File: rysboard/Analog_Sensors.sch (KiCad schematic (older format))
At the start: 16 parts

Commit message: cleanup
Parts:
- added D18, D19, D20: D_TVS, symbol Device:D_TVS
- added R62, R63, R64, R65, R66, R67: R, symbol Device:R
- J14: renamed from J?; value Conn_01x02 -> BAT2_TH
- J21: renamed from J?; value Conn_01x02 -> BAT3_TH
- J8: renamed from J?; value Conn_01x02 -> BAT1_TH
- gave numbers to parts that had none: 13
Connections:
- net BAT_T_1: now also J8.2 (Pin_2), R54.2
- net BAT_T_2: now also J14.2 (Pin_2), R58.2
- net BAT_T_3: now also J21.2 (Pin_2), R60.2
- net BOARD_T_1: now also R55.2, TH2.1
- net BOARD_T_2: now also R59.2, TH3.1
- net BOARD_T_3: now also R61.2, TH4.1
- net GND: now also J14.1 (Pin_1), J21.1 (Pin_1), J8.1 (Pin_1), D18.2 (A2), D19.2 (A2), D20.2 (A2), R63.2, R65.2, R67.2; no longer J14.2 (Pin_2), J21.2 (Pin_2), J8.2 (Pin_2)
- net V_BAT_C1: now also D18.1 (A1), R62.2, R63.1
- net V_BAT_C2: now also D19.1 (A1), R64.2, R65.1
- net V_BAT_C3: now also D20.1 (A1), R66.2, R67.1
- net V_CELL1: now also R62.1
- net V_CELL2: now also R64.1
- net V_CELL3: now also R66.1
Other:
- note added: "0-10V\n"
- note added: "0-15V\n"
- note added: "0-5V\n"
- moved on the sheet: R54, R58, R60

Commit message: first modyfications in St Motor section
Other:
- note added: "33v == 3.3v\n\nR=U/I\nI=U/R1+R2\nR1 =90KOhm\nR2 = 10KOhm\n\n9.9 == 3.3V\nR1 = 10KOhm\nR2 = 5KOhm"
- note removed: "33v == 3.3v\n\nR=U/I\nI=U/R1+R2\nR1 =10KOhm\nR2 = 90KOhm\n\n9.9 == 3.3V\nR1 = 10KOhm\nR2 = 20 KOhm"
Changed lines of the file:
@@
 $EndComp
 Text Notes 3950 4850 0    50   ~ 0
-33v == 3.3v\n\nR=U/I\nI=U/R1+R2\nR1 =10KOhm\nR2 = 90KOhm\n\n9.9 == 3.3V\nR1 = 10KOhm\nR2 =  20 KOhm
+33v == 3.3v\n\nR=U/I\nI=U/R1+R2\nR1 =90KOhm\nR2 = 10KOhm\n\n9.9 == 3.3V\nR1 = 10KOhm\nR2 =  5KOhm
 Text Notes 3900 3900 0    50   ~ 0
 TO DO:\nDouble check values\n

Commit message: sensors enable added, Vref problem to solve
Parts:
- removed D18, D19, D20: D_TVS, symbol Device:D_TVS
- removed R55, R56, R57, R59, R61, R64, R66: R, symbol Device:R
- added Q?: IRLML6402, Package_TO_SOT_SMD:SOT-23, symbol Transistor_FET:IRLML6402
- added R? (x7): 10KR, symbol Device:R
- added R?: 5KR, symbol Device:R
- added R?: 100KR, symbol Device:R
- R52: value 90KR0.5% -> 9KR0.5%
- R53: value 10KR0.5% -> 1KR0.5%
- R62: value R -> 10KR
- R63: value R -> 20KR
- R65: value R -> 5KR
- R67: value R -> 2.8KR
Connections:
- net +5V: now also R?.1
- net BOARD_T_1: now also R?.2
- net BOARD_T_2: now also R?.2
- net BOARD_T_3: now also R?.2
- net GND: now also R?.2
- net MCU_3.3V: now also Q?.2 (S), R?.1; no longer R54.1, R58.1, R60.1
- net V_BAT_C2: now also R?.2
- net V_BAT_C3: now also R?.2
- net V_CELL2: now also R?.1
- net V_CELL3: now also R?.1
- net V_P_5: now also R?.1, R?.2
- new net: Q?.1 (G), R?.1, R?.2
- new net MCU_Sensor_3.3V: Q?.3 (D), R54.1, R58.1, R60.1, R?.1, R?.1, R?.1
- new net S_E: R?.2
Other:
- note added: "0-15.086V\n"
- note added: "0-4.95V\n"
- note added: "0-9.9V\n"
- note added: "When not used, thermistors do not need to be powered on."
- note removed: "0-10V\n"
- note removed: "0-15V\n"
- note removed: "0-5V\n"
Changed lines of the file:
@@
 	1    0    0    -1
 $EndComp
-Text GLabel 3350 950  1    50   Output ~ 0
-MCU_3.3V
-Text GLabel 2550 950  1    50   Output ~ 0
-MCU_3.3V
-Text GLabel 4150 950  1    50   Output ~ 0
-MCU_3.3V
 $Comp
 L Connector_Generic:Conn_01x02 J8
@@
 	0    -1   -1   0
 $EndComp
-$Comp
-L Device:R R55
-U 1 1 603EEB5E
-P 2750 2200
-F 0 "R55" H 2820 2246 50  0000 L CNN
-F 1 "R" H 2820 2155 50  0000 L CNN
-F 2 "" V 2680 2200 50  0001 C CNN
-F 3 "~" H 2750 2200 50  0001 C CNN
-	1    2750 2200
-	1    0    0    -1
-$EndComp
-Text GLabel 2600 2000 0    50   Output ~ 0
-MCU_3.3V
-$Comp
-L Device:R R59
-U 1 1 603EEFA0
-P 3400 2200
-F 0 "R59" H 3470 2246 50  0000 L CNN
-F 1 "R" H 3470 2155 50  0000 L CNN
-F 2 "" V 3330 2200 50  0001 C CNN
-F 3 "~" H 3400 2200 50  0001 C CNN
-	1    3400 2200
-	1    0    0    -1
-$EndComp
-$Comp
-L Device:R R61
-U 1 1 603EF182
-P 4200 2200
-F 0 "R61" H 4270 2246 50  0000 L CNN
-F 1 "R" H 4270 2155 50  0000 L CNN
-F 2 "" V 4130 2200 50  0001 C CNN
-F 3 "~" H 4200 2200 50  0001 C CNN
-	1    4200 2200
-	1    0    0    -1
-$EndComp
 Wire Wire Line
 	2600 2000 2750 2000
@@
 P 2050 4400
 F 0 "R52" H 2120 4446 50  0000 L CNN
-F 1 "90KR0.5%" H 2120 4355 50  0000 L CNN
+F 1 "9KR0.5%" H 2120 4355 50  0000 L CNN
 F 2 "" V 1980 4400 50  0001 C CNN
 F 3 "~" H 2050 4400 50  0001 C CNN
@@
 P 2050 4700
 F 0 "R53" H 1980 4654 50  0000 R CNN
-F 1 "10KR0.5%" H 1980 4745 50  0000 R CNN
+F 1 "1KR0.5%" H 1980 4745 50  0000 R CNN
 F 2 "" V 1980 4700 50  0001 C CNN
 F 3 "~" H 2050 4700 50  0001 C CNN
@@
 Connection ~ 2050 4550
 $Comp
-L Device:R R56
-U 1 1 60408D6C
-P 3150 4400
-F 0 "R56" H 3220 4446 50  0000 L CNN
-F 1 "R" H 3220 4355 50  0000 L CNN
-F 2 "" V 3080 4400 50  0001 C CNN
-F 3 "~" H 3150 4400 50  0001 C CNN
-	1    3150 4400
-	1    0    0    -1
-$EndComp
-$Comp
-L Device:R R57
-U 1 1 604091C5
-P 3150 4700
-F 0 "R57" H 3220 4746 50  0000 L CNN
-F 1 "R" H 3220 4655 50  0000 L CNN
-F 2 "" V 3080 4700 50  0001 C CNN
-F 3 "~" H 3150 4700 50  0001 C CNN
-	1    3150 4700
-	1    0    0    -1
-$EndComp
-Connection ~ 3150 4550
-$Comp
 L power:GND #PWR052
 U 1 1 604093E1
@@
 P 6250 4400
 F 0 "R62" H 6320 4446 50  0000 L CNN
-F 1 "R" H 6320 4355 50  0000 L CNN
+F 1 "10KR" H 6320 4355 50  0000 L CNN
 F 2 "" V 6180 4400 50  0001 C CNN
 F 3 "~" H 6250 4400 50  0001 C CNN
@@
 P 6250 4700
 F 0 "R63" H 6320 4746 50  0000 L CNN
-F 1 "R" H 6320 4655 50  0000 L CNN
+F 1 "20KR" H 6320 4655 50  0000 L CNN
 F 2 "" V 6180 4700 50  0001 C CNN
 F 3 "~" H 6250 4700 50  0001 C CNN
 	1    6250 4700
-	1    0    0    -1
-$EndComp
-$Comp
-L Device:R R64
-U 1 1 6037FF91
-P 7050 4400
-F 0 "R64" H 7120 4446 50  0000 L CNN
-F 1 "R" H 7120 4355 50  0000 L CNN
-F 2 "" V 6980 4400 50  0001 C CNN
-F 3 "~" H 7050 4400 50  0001 C CNN
-	1    7050 4400
 	1    0    0    -1
 $EndComp
@@
 P 7050 4700
 F 0 "R65" H 7120 4746 50  0000 L CNN
-F 1 "R" H 7120 4655 50  0000 L CNN
+F 1 "5KR" H 7120 4655 50  0000 L CNN
 F 2 "" V 6980 4700 50  0001 C CNN
 F 3 "~" H 7050 4700 50  0001 C CNN
 	1    7050 4700
-	1    0    0    -1
-$EndComp
-$Comp
-L Device:R R66
-U 1 1 603802FE
-P 7850 4400
-F 0 "R66" H 7920 4446 50  0000 L CNN
-F 1 "R" H 7920 4355 50  0000 L CNN
-F 2 "" V 7780 4400 50  0001 C CNN
-F 3 "~" H 7850 4400 50  0001 C CNN
-	1    7850 4400
 	1    0    0    -1
 $EndComp
@@
 P 7850 4700
 F 0 "R67" H 7920 4746 50  0000 L CNN
-F 1 "R" H 7920 4655 50  0000 L CNN
+F 1 "2.8KR" H 7920 4655 50  0000 L CNN
 F 2 "" V 7780 4700 50  0001 C CNN
 F 3 "~" H 7850 4700 50  0001 C CNN
@@
 $EndComp
 Text Notes 6250 3650 0    50   ~ 0
-0-5V\n
+0-4.95V\n
 Text Notes 6950 3650 0    50   ~ 0
-0-10V\n
+0-9.9V\n
 Text Notes 7750 3650 0    50   ~ 0
-0-15V\n
-$Comp
-L Device:D_TVS D18
-U 1 1 60385CF5
-P 6500 4700
-F 0 "D18" V 6454 4780 50  0000 L CNN
-F 1 "D_TVS" V 6545 4780 50  0000 L CNN
-F 2 "" H 6500 4700 50  0001 C CNN
-F 3 "~" H 6500 4700 50  0001 C CNN
-	1    6500 4700
-	0    1    1    0
-$EndComp
-$Comp
-L Device:D_TVS D19
-U 1 1 603861A1
-P 7300 4700
-F 0 "D19" V 7254 4780 50  0000 L CNN
-F 1 "D_TVS" V 7345 4780 50  0000 L CNN
-F 2 "" H 7300 4700 50  0001 C CNN
-F 3 "~" H 7300 4700 50  0001 C CNN
-	1    7300 4700
-	0    1    1    0
-$EndComp
-$Comp
-L Device:D_TVS D20
-U 1 1 6038637D
-P 8100 4700
-F 0 "D20" V 8054 4780 50  0000 L CNN
-F 1 "D_TVS" V 8145 4780 50  0000 L CNN
-F 2 "" H 8100 4700 50  0001 C CNN
-F 3 "~" H 8100 4700 50  0001 C CNN
-	1    8100 4700
-	0    1    1    0
-$EndComp
-Wire Wire Line
-	8100 4850 7850 4850
-Connection ~ 7850 4850
-Wire Wire Line
-	8100 4550 7850 4550
-Connection ~ 7850 4550
-Wire Wire Line
-	7300 4550 7050 4550
-Connection ~ 7050 4550
-Wire Wire Line
-	7300 4850 7050 4850
-Connection ~ 7050 4850
-Wire Wire Line
-	6500 4550 6250 4550
-Connection ~ 6250 4550
-Wire Wire Line
-	6500 4850 6250 4850
-Connection ~ 6250 4850
+0-15.086V\n
 Text HLabel 2500 1300 0    50   Input ~ 0
 BAT_T_1
@@
 	4150 1300 4150 1350
 Connection ~ 4150 1300
+$Comp
+L Device:R R?
+U 1 1 603B8902
+P 7050 4400
+F 0 "R?" H 7120 4446 50  0000 L CNN
+F 1 "10KR" H 7120 4355 50  0000 L CNN
+F 2 "" V 6980 4400 50  0001 C CNN
+F 3 "~" H 7050 4400 50  0001 C CNN
+	1    7050 4400
+	1    0    0    -1
+$EndComp
+$Comp
+L Device:R R?
+U 1 1 603B8D2E
+P 7850 4400
+F 0 "R?" H 7920 4446 50  0000 L CNN
+F 1 "10KR" H 7920 4355 50  0000 L CNN
+F 2 "" V 7780 4400 50  0001 C CNN
+F 3 "~" H 7850 4400 50  0001 C CNN
+	1    7850 4400
+	1    0    0    -1
+$EndComp
+$Comp
+L Device:R R?
+U 1 1 603B9257
+P 3150 4400
+F 0 "R?" H 3220 4446 50  0000 L CNN
+F 1 "10KR" H 3220 4355 50  0000 L CNN
+F 2 "" V 3080 4400 50  0001 C CNN
+F 3 "~" H 3150 4400 50  0001 C CNN
+	1    3150 4400
+	1    0    0    -1
+$EndComp
+$Comp
+L Device:R R?
+U 1 1 603B976E
+P 3150 4700
+F 0 "R?" H 3220 4746 50  0000 L CNN
+F 1 "5KR" H 3220 4655 50  0000 L CNN
+F 2 "" V 3080 4700 50  0001 C CNN
+F 3 "~" H 3150 4700 50  0001 C CNN
+	1    3150 4700
+	1    0    0    -1
+$EndComp
+Connection ~ 3150 4550
+Text GLabel 6150 1100 1    50   Output ~ 0
+MCU_3.3V
+Text Label 2600 2000 0    50   ~ 0
+MCU_Sensor_3.3V
+Text Label 1900 900  0    50   ~ 0
+MCU_Sensor_3.3V
+Wire Wire Line
+	1900 900  2550 900
+Wire Wire Line
+	2550 900  2550 950
+Text Label 2750 900  0    50   ~ 0
+MCU_Sensor_3.3V
+Wire Wire Line
+	2750 900  3350 900
+Wire Wire Line
+	3350 900  3350 950
+Text Label 3550 900  0    50   ~ 0
+MCU_Sensor_3.3V
+Wire Wire Line
+	3550 900  4150 900
+Wire Wire Line
+	4150 900  4150 950
+Text Label 7150 1600 0    50   ~ 0
+MCU_Sensor_3.3V
+$Comp
+L Device:R R?
+U 1 1 603BD637
+P 2750 2200
+F 0 "R?" H 2820 2246 50  0000 L CNN
+F 1 "10KR" H 2820 2155 50  0000 L CNN
+F 2 "" V 2680 2200 50  0001 C CNN
+F 3 "~" H 2750 2200 50  0001 C CNN
+	1    2750 2200
+	1    0    0    -1
+$EndComp
+$Comp
+L Device:R R?
+U 1 1 603BDD9E
+P 3400 2200
+F 0 "R?" H 3470 2246 50  0000 L CNN
+F 1 "10KR" H 3470 2155 50  0000 L CNN
+F 2 "" V 3330 2200 50  0001 C CNN
+F 3 "~" H 3400 2200 50  0001 C CNN
+	1    3400 2200
+	1    0    0    -1
+$EndComp
+$Comp
+L Device:R R?
+U 1 1 603BDFD4
+P 4200 2200
+F 0 "R?" H 4270 2246 50  0000 L CNN
+F 1 "10KR" H 4270 2155 50  0000 L CNN
+F 2 "" V 4130 2200 50  0001 C CNN
+F 3 "~" H 4200 2200 50  0001 C CNN
+	1    4200 2200
+	1    0    0    -1
+$EndComp
+$Comp
+L Transistor_FET:IRLML6402 Q?
+U 1 1 603BF81C
+P 6650 1400
+F 0 "Q?" H 6854 1354 50  0000 L CNN
+F 1 "IRLML6402" H 6854 1445 50  0000 L CNN
+F 2 "Package_TO_SOT_SMD:SOT-23" H 6850 1325 50  0001 L CIN
+F 3 "https://www.infineon.com/dgdl/irlml6402pbf.pdf?fileId=5546d462533600a401535668d5c2263c" H 6650 1400 50  0001 L CNN
+	1    6650 1400
+	1    0    0    1
+$EndComp
+Wire Wire Line
+	7150 1600 6750 1600
+Wire Wire Line
+	6150 1100 6300 1100
+Wire Wire Line
+	6750 1100 6750 1200
+$Comp
+L Device:R R?
+U 1 1 603C19CD
+P 6300 1250
+F 0 "R?" H 6370 1296 50  0000 L CNN
+F 1 "100KR" H 6370 1205 50  0000 L CNN
+F 2 "" V 6230 1250 50  0001 C CNN
+F 3 "~" H 6300 1250 50  0001 C CNN
+	1    6300 1250
+	1    0    0    -1
+$EndComp
+Connection ~ 6300 1100
+Wire Wire Line
+	6300 1100 6750 1100
+$Comp
+L Device:R R?
+U 1 1 603C1DE2
+P 6150 1400
+F 0 "R?" H 6220 1446 50  0000 L CNN
+F 1 "10KR" H 6220 1355 50  0000 L CNN
+F 2 "" V 6080 1400 50  0001 C CNN
+F 3 "~" H 6150 1400 50  0001 C CNN
+	1    6150 1400
+	0    1    1    0
+$EndComp
+Wire Wire Line
+	6300 1400 6450 1400
+Connection ~ 6300 1400
+Text HLabel 5850 1400 0    50   Input ~ 0
+S_E
+Wire Wire Line
+	5850 1400 6000 1400
+Text Notes 8450 1000 0    50   ~ 0
+When not used, thermistors do not need to be powered on.
 $EndSCHEMATC

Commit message: new mosfet footprints
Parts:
- R52, R53, R62, R63, R65, R67: footprint (none) -> Resistor_SMD:R_0603_1608Metric
- R54, R58, R60: value R -> 10KR; footprint (none) -> Resistor_SMD:R_0603_1608Metric
- R55, R56, R57, R59, R61, R64, R66, R70, R71: renamed from R?; footprint (none) -> Resistor_SMD:R_0603_1608Metric
- TH2, TH3, TH4: footprint (none) -> Resistor_SMD:R_0805_2012Metric_Pad1.15x1.40mm_HandSolder
- gave numbers to parts that had none: 1
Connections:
- net MCU_Sensor_3.3V renamed 3_3V_REF
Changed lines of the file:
@@
 V_BAT_C3
-$Comp
-L Device:R R54
-U 1 1 603E581F
-P 2550 1100
-F 0 "R54" H 2620 1146 50  0000 L CNN
-F 1 "R" H 2620 1055 50  0000 L CNN
-F 2 "" V 2480 1100 50  0001 C CNN
-F 3 "~" H 2550 1100 50  0001 C CNN
-	1    2550 1100
-	1    0    0    -1
-$EndComp
-$Comp
-L Device:R R58
-U 1 1 603E5A74
-P 3350 1100
-F 0 "R58" H 3420 1146 50  0000 L CNN
-F 1 "R" H 3420 1055 50  0000 L CNN
-F 2 "" V 3280 1100 50  0001 C CNN
-F 3 "~" H 3350 1100 50  0001 C CNN
-	1    3350 1100
-	1    0    0    -1
-$EndComp
-$Comp
-L Device:R R60
-U 1 1 603E5B7A
-P 4150 1100
-F 0 "R60" H 4220 1146 50  0000 L CNN
-F 1 "R" H 4220 1055 50  0000 L CNN
-F 2 "" V 4080 1100 50  0001 C CNN
-F 3 "~" H 4150 1100 50  0001 C CNN
-	1    4150 1100
-	1    0    0    -1
-$EndComp
 $Comp
 L Connector_Generic:Conn_01x02 J8
@@
 F 0 "TH2" H 2848 2546 50  0000 L CNN
 F 1 "Thermistor_PTC" H 2848 2455 50  0000 L CNN
-F 2 "" H 2800 2300 50  0001 L CNN
+F 2 "Resistor_SMD:R_0805_2012Metric_Pad1.15x1.40mm_HandSolder" H 2800 2300 50  0001 L CNN
 F 3 "~" H 2750 2500 50  0001 C CNN
 	1    2750 2500
@@
 F 0 "TH3" H 3498 2546 50  0000 L CNN
 F 1 "Thermistor_PTC" H 3498 2455 50  0000 L CNN
-F 2 "" H 3450 2300 50  0001 L CNN
+F 2 "Resistor_SMD:R_0805_2012Metric_Pad1.15x1.40mm_HandSolder" H 3450 2300 50  0001 L CNN
 F 3 "~" H 3400 2500 50  0001 C CNN
 	1    3400 2500
@@
 F 0 "TH4" H 4298 2546 50  0000 L CNN
 F 1 "Thermistor_PTC" H 4298 2455 50  0000 L CNN
-F 2 "" H 4250 2300 50  0001 L CNN
+F 2 "Resistor_SMD:R_0805_2012Metric_Pad1.15x1.40mm_HandSolder" H 4250 2300 50  0001 L CNN
 F 3 "~" H 4200 2500 50  0001 C CNN
 	1    4200 2500
@@
 F 0 "R52" H 2120 4446 50  0000 L CNN
 F 1 "9KR0.5%" H 2120 4355 50  0000 L CNN
-F 2 "" V 1980 4400 50  0001 C CNN
+F 2 "Resistor_SMD:R_0603_1608Metric" V 1980 4400 50  0001 C CNN
 F 3 "~" H 2050 4400 50  0001 C CNN
 	1    2050 4400
@@
 F 0 "R53" H 1980 4654 50  0000 R CNN
 F 1 "1KR0.5%" H 1980 4745 50  0000 R CNN
-F 2 "" V 1980 4700 50  0001 C CNN
+F 2 "Resistor_SMD:R_0603_1608Metric" V 1980 4700 50  0001 C CNN
 F 3 "~" H 2050 4700 50  0001 C CNN
 	1    2050 4700
@@
 F 0 "R62" H 6320 4446 50  0000 L CNN
 F 1 "10KR" H 6320 4355 50  0000 L CNN
-F 2 "" V 6180 4400 50  0001 C CNN
+F 2 "Resistor_SMD:R_0603_1608Metric" V 6180 4400 50  0001 C CNN
 F 3 "~" H 6250 4400 50  0001 C CNN
 	1    6250 4400
@@
 F 0 "R63" H 6320 4746 50  0000 L CNN
 F 1 "20KR" H 6320 4655 50  0000 L CNN
-F 2 "" V 6180 4700 50  0001 C CNN
+F 2 "Resistor_SMD:R_0603_1608Metric" V 6180 4700 50  0001 C CNN
 F 3 "~" H 6250 4700 50  0001 C CNN
 	1    6250 4700
@@
 F 0 "R65" H 7120 4746 50  0000 L CNN
 F 1 "5KR" H 7120 4655 50  0000 L CNN
-F 2 "" V 6980 4700 50  0001 C CNN
+F 2 "Resistor_SMD:R_0603_1608Metric" V 6980 4700 50  0001 C CNN
 F 3 "~" H 7050 4700 50  0001 C CNN
 	1    7050 4700
@@
 F 0 "R67" H 7920 4746 50  0000 L CNN
 F 1 "2.8KR" H 7920 4655 50  0000 L CNN
-F 2 "" V 7780 4700 50  0001 C CNN
+F 2 "Resistor_SMD:R_0603_1608Metric" V 7780 4700 50  0001 C CNN
 F 3 "~" H 7850 4700 50  0001 C CNN
 	1    7850 4700
@@
 Connection ~ 4150 1300
 $Comp
-L Device:R R?
+L Device:R R70
 U 1 1 603B8902
 P 7050 4400
-F 0 "R?" H 7120 4446 50  0000 L CNN
+F 0 "R70" H 7120 4446 50  0000 L CNN
 F 1 "10KR" H 7120 4355 50  0000 L CNN
-F 2 "" V 6980 4400 50  0001 C CNN
+F 2 "Resistor_SMD:R_0603_1608Metric" V 6980 4400 50  0001 C CNN
 F 3 "~" H 7050 4400 50  0001 C CNN
 	1    7050 4400
@@
 $EndComp
 $Comp
-L Device:R R?
+L Device:R R71
 U 1 1 603B8D2E
 P 7850 4400
-F 0 "R?" H 7920 4446 50  0000 L CNN
+F 0 "R71" H 7920 4446 50  0000 L CNN
 F 1 "10KR" H 7920 4355 50  0000 L CNN
-F 2 "" V 7780 4400 50  0001 C CNN
+F 2 "Resistor_SMD:R_0603_1608Metric" V 7780 4400 50  0001 C CNN
 F 3 "~" H 7850 4400 50  0001 C CNN
 	1    7850 4400
@@
 $EndComp
 $Comp
-L Device:R R?
+L Device:R R56
 U 1 1 603B9257
 P 3150 4400
-F 0 "R?" H 3220 4446 50  0000 L CNN
+F 0 "R56" H 3220 4446 50  0000 L CNN
 F 1 "10KR" H 3220 4355 50  0000 L CNN
-F 2 "" V 3080 4400 50  0001 C CNN
+F 2 "Resistor_SMD:R_0603_1608Metric" V 3080 4400 50  0001 C CNN
 F 3 "~" H 3150 4400 50  0001 C CNN
 	1    3150 4400
@@
 $EndComp
 $Comp
-L Device:R R?
+L Device:R R57
 U 1 1 603B976E
 P 3150 4700
-F 0 "R?" H 3220 4746 50  0000 L CNN
+F 0 "R57" H 3220 4746 50  0000 L CNN
 F 1 "5KR" H 3220 4655 50  0000 L CNN
-F 2 "" V 3080 4700 50  0001 C CNN
+F 2 "Resistor_SMD:R_0603_1608Metric" V 3080 4700 50  0001 C CNN
 F 3 "~" H 3150 4700 50  0001 C CNN
 	1    3150 4700
@@
 MCU_Sensor_3.3V
 $Comp
-L Device:R R?
+L Device:R R55
 U 1 1 603BD637
 P 2750 2200
-F 0 "R?" H 2820 2246 50  0000 L CNN
+F 0 "R55" H 2820 2246 50  0000 L CNN
 F 1 "10KR" H 2820 2155 50  0000 L CNN
-F 2 "" V 2680 2200 50  0001 C CNN
+F 2 "Resistor_SMD:R_0603_1608Metric" V 2680 2200 50  0001 C CNN
 F 3 "~" H 2750 2200 50  0001 C CNN
 	1    2750 2200
@@
 $EndComp
 $Comp
-L Device:R R?
+L Device:R R59
 U 1 1 603BDD9E
 P 3400 2200
-F 0 "R?" H 3470 2246 50  0000 L CNN
+F 0 "R59" H 3470 2246 50  0000 L CNN
 F 1 "10KR" H 3470 2155 50  0000 L CNN
-F 2 "" V 3330 2200 50  0001 C CNN
+F 2 "Resistor_SMD:R_0603_1608Metric" V 3330 2200 50  0001 C CNN
 F 3 "~" H 3400 2200 50  0001 C CNN
 	1    3400 2200
@@
 $EndComp
 $Comp
-L Device:R R?
+L Device:R R61
 U 1 1 603BDFD4
 P 4200 2200
-F 0 "R?" H 4270 2246 50  0000 L CNN
+F 0 "R61" H 4270 2246 50  0000 L CNN
 F 1 "10KR" H 4270 2155 50  0000 L CNN
-F 2 "" V 4130 2200 50  0001 C CNN
+F 2 "Resistor_SMD:R_0603_1608Metric" V 4130 2200 50  0001 C CNN
 F 3 "~" H 4200 2200 50  0001 C CNN
 	1    4200 2200
@@
 $EndComp
 $Comp
-L Transistor_FET:IRLML6402 Q?
+L Transistor_FET:IRLML6402 Q12
 U 1 1 603BF81C
 P 6650 1400
-F 0 "Q?" H 6854 1354 50  0000 L CNN
+F 0 "Q12" H 6854 1354 50  0000 L CNN
 F 1 "IRLML6402" H 6854 1445 50  0000 L CNN
 F 2 "Package_TO_SOT_SMD:SOT-23" H 6850 1325 50  0001 L CIN
@@
 	6750 1100 6750 1200
 $Comp
-L Device:R R?
+L Device:R R66
 U 1 1 603C19CD
 P 6300 1250
-F 0 "R?" H 6370 1296 50  0000 L CNN
+F 0 "R66" H 6370 1296 50  0000 L CNN
 F 1 "100KR" H 6370 1205 50  0000 L CNN
-F 2 "" V 6230 1250 50  0001 C CNN
+F 2 "Resistor_SMD:R_0603_1608Metric" V 6230 1250 50  0001 C CNN
 F 3 "~" H 6300 1250 50  0001 C CNN
 	1    6300 1250
@@
 	6300 1100 6750 1100
 $Comp
-L Device:R R?
+L Device:R R64
 U 1 1 603C1DE2
 P 6150 1400
-F 0 "R?" H 6220 1446 50  0000 L CNN
+F 0 "R64" H 6220 1446 50  0000 L CNN
 F 1 "10KR" H 6220 1355 50  0000 L CNN
-F 2 "" V 6080 1400 50  0001 C CNN
+F 2 "Resistor_SMD:R_0603_1608Metric" V 6080 1400 50  0001 C CNN
 F 3 "~" H 6150 1400 50  0001 C CNN
 	1    6150 1400
@@
 Text Notes 8450 1000 0    50   ~ 0
 When not used, thermistors do not need to be powered on.
+$Comp
+L Device:R R54
+U 1 1 603FD549
+P 2550 1100
+F 0 "R54" H 2620 1146 50  0000 L CNN
+F 1 "10KR" H 2620 1055 50  0000 L CNN
+F 2 "Resistor_SMD:R_0603_1608Metric" V 2480 1100 50  0001 C CNN
+F 3 "~" H 2550 1100 50  0001 C CNN
+	1    2550 1100
+	1    0    0    -1
+$EndComp
+$Comp
+L Device:R R58
+U 1 1 603FD808
+P 3350 1100
+F 0 "R58" H 3420 1146 50  0000 L CNN
+F 1 "10KR" H 3420 1055 50  0000 L CNN
+F 2 "Resistor_SMD:R_0603_1608Metric" V 3280 1100 50  0001 C CNN
+F 3 "~" H 3350 1100 50  0001 C CNN
+	1    3350 1100
+	1    0    0    -1
+$EndComp
+$Comp
+L Device:R R60
+U 1 1 603FDA2E
+P 4150 1100
+F 0 "R60" H 4220 1146 50  0000 L CNN
+F 1 "10KR" H 4220 1055 50  0000 L CNN
+F 2 "Resistor_SMD:R_0603_1608Metric" V 4080 1100 50  0001 C CNN
+F 3 "~" H 4150 1100 50  0001 C CNN
+	1    4150 1100
+	1    0    0    -1
+$EndComp
+Text HLabel 6950 1600 3    50   Input ~ 0
+3_3V_REF
 $EndSCHEMATC

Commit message: Fixed library, added a few MOSFET layouts
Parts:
- removed Q12: IRLML6402, Package_TO_SOT_SMD:SOT-23, symbol Transistor_FET:IRLML6402
- added Q?: DMP2075UFDB, SamacSys_Parts:DMP2075UFDB7, symbol rysboard:DMP2075UFDB
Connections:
- net 3_3V_REF: now also Q?.3 (S2), Q?.8 (D2_2)
- net MCU_3.3V: now also Q?.3 (S2)
- net at R64.1, R66.2: now also Q?.4 (G2)
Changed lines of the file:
@@
 	1    0    0    -1
-$EndComp
-$Comp
-L Transistor_FET:IRLML6402 Q12
-U 1 1 603BF81C
-P 6650 1400
-F 0 "Q12" H 6854 1354 50  0000 L CNN
-F 1 "IRLML6402" H 6854 1445 50  0000 L CNN
-F 2 "Package_TO_SOT_SMD:SOT-23" H 6850 1325 50  0001 L CIN
-F 3 "https://www.infineon.com/dgdl/irlml6402pbf.pdf?fileId=5546d462533600a401535668d5c2263c" H 6650 1400 50  0001 L CNN
-	1    6650 1400
-	1    0    0    1
 $EndComp
 Wire Wire Line
@@
 Text HLabel 6950 1600 3    50   Input ~ 0
 3_3V_REF
+$Comp
+L rysboard:DMP2075UFDB Q?
+U 2 1 605EDFDE
+P 6650 1400
+F 0 "Q?" H 6855 1354 50  0000 L CNN
+F 1 "DMP2075UFDB" H 6855 1445 50  0000 L CNN
+F 2 "SamacSys_Parts:DMP2075UFDB7" H 6850 1325 50  0001 L CIN
+F 3 "" H 6650 1400 50  0001 L CNN
+	2    6650 1400
+	1    0    0    1
+$EndComp
 $EndSCHEMATC

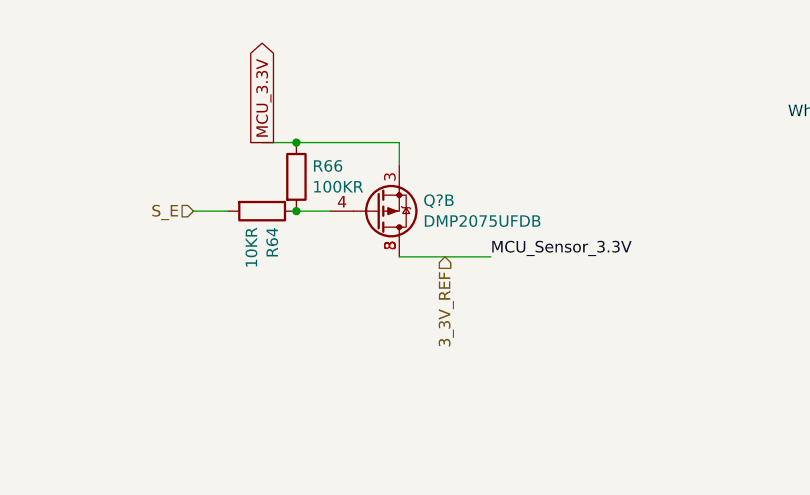
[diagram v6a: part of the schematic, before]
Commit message: battery Balancing specified
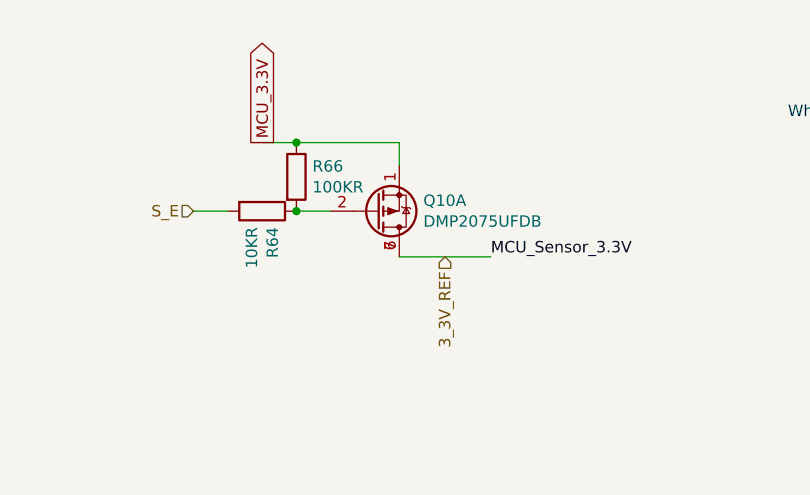
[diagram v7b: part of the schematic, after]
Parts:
- gave numbers to parts that had none: 1
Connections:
- net 3_3V_REF: now also Q10.6 (D2_2), Q10.7 (D2_2); no longer Q10.3 (S2), Q10.8 (D2_2)
- net MCU_3.3V: now also Q10.1 (S1); no longer Q10.3 (S2)
- net at R64.1, R66.2: now also Q10.2 (G1); no longer Q10.4 (G2)
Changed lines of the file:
@@
 3_3V_REF
 $Comp
-L rysboard:DMP2075UFDB Q?
-U 2 1 605EDFDE
+L rysboard:DMP2075UFDB Q10
+U 1 1 605EDFDE
 P 6650 1400
-F 0 "Q?" H 6855 1354 50  0000 L CNN
+F 0 "Q10" H 6855 1354 50  0000 L CNN
 F 1 "DMP2075UFDB" H 6855 1445 50  0000 L CNN
 F 2 "SamacSys_Parts:DMP2075UFDB7" H 6850 1325 50  0001 L CIN
 F 3 "" H 6650 1400 50  0001 L CNN
-	2    6650 1400
+	1    6650 1400
 	1    0    0    1
 $EndComp
